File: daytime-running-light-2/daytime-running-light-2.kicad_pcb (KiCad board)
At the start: 2 copper layers, 57.8 x 87.8 mm, 58 parts, among them J1 Conn_01x01_Socket, J2 Conn_01x01_Socket, J3 Conn_01x01_Socket, J4 Conn_01x01_Socket, J5 Conn_01x01_Socket, J6 Conn_01x01_Pin, J7 Conn_01x01_Socket, J8 Conn_01x01_Socket, J9 Conn_01x01_Socket, Q1 BC548, Q2 IRF9540N, Q3 IRFB3004PbF, SW1 SW_SPST, U1 L7812, U2 TLC555xP, U3 L7812, U4 4001, U5 4069, U6 IRS10752LPbF

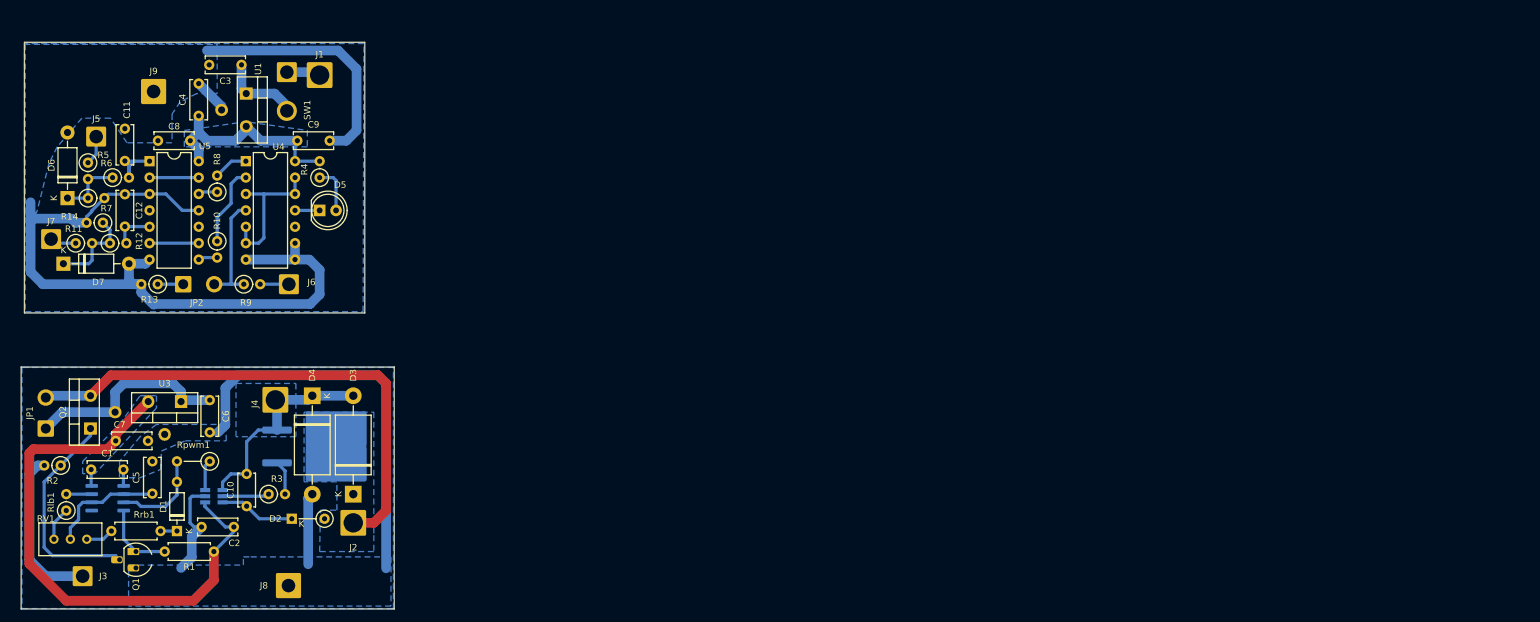
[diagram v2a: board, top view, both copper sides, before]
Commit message: [drl] Add proper voltage bootstrap powered from a double voltage. Start reimpl PCB
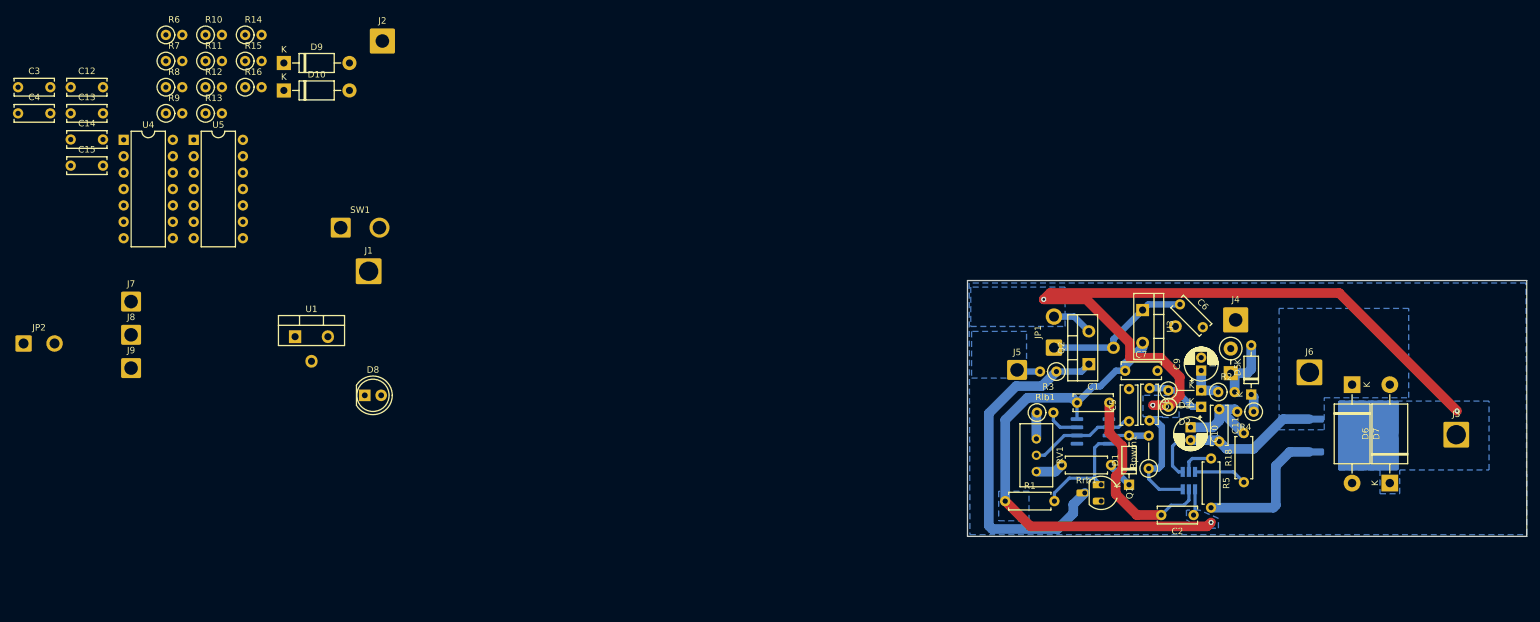
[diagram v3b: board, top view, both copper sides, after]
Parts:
- added C13: 0.1uF, Capacitor_THT:C_Disc_D6.0mm_W2.5mm_P5.00mm, F.Cu at (27.2, 29.7)
- added C14: 0.33uF, Capacitor_THT:C_Disc_D6.0mm_W2.5mm_P5.00mm, F.Cu at (27.2, 33.8)
- added C15: 0.33uF, Capacitor_THT:C_Disc_D6.0mm_W2.5mm_P5.00mm, F.Cu at (27.2, 37.8)
- added D10: 1N4742A, Diode_THT:D_DO-41_SOD81_P10.16mm_Horizontal, F.Cu at (60.2, 26.2)
- added D8: LED, LED_THT:LED_D5.0mm, F.Cu at (72.8, 73.4)
- added D9: 1N47xxA, Diode_THT:D_DO-41_SOD81_P10.16mm_Horizontal, F.Cu at (60.2, 21.9)
- added R15: R, Resistor_THT:R_Axial_DIN0207_L6.3mm_D2.5mm_P2.54mm_Vertical, F.Cu at (54.3, 21.6)
- added R16: 100k, Resistor_THT:R_Axial_DIN0207_L6.3mm_D2.5mm_P2.54mm_Vertical, F.Cu at (54.3, 25.7)
- added R18: 0R, Resistor_THT:R_Axial_DIN0207_L6.3mm_D2.5mm_P7.62mm_Horizontal, F.Cu at (208.9, 86.9)
- C10: value C -> 4.7uF; footprint Capacitor_THT:C_Disc_D5.0mm_W2.5mm_P5.00mm -> Capacitor_THT:CP_Radial_D5.0mm_P2.00mm
- C11: value 0.33uF -> 100nF
- C12: value 0.33uF -> 0.1uF
- C8: value 0.1uF -> 100nF
- C9: value 0.1uF -> 1uF; footprint Capacitor_THT:C_Disc_D6.0mm_W2.5mm_P5.00mm -> Capacitor_THT:CP_Radial_D5.0mm_P2.00mm
- D2: value 1N4148 -> BAT42
- D3: value 1.5KE18A -> BAT42; footprint Diode_THT:D_DO-201AE_P15.24mm_Horizontal -> Diode_THT:D_DO-35_SOD27_P5.08mm_Vertical_KathodeUp
- D4: value 1.5KE18A -> 1N4746A, 18V; footprint Diode_THT:D_DO-201AE_P15.24mm_Horizontal -> Diode_THT:D_DO-41_SOD81_P3.81mm_Vertical_KathodeUp
- D5: value LED -> 1N4148; footprint LED_THT:LED_D5.0mm -> Diode_THT:D_DO-35_SOD27_P7.62mm_Horizontal
- D6: value 1N47xxA -> 1.5KE18A; footprint Diode_THT:D_DO-41_SOD81_P10.16mm_Horizontal -> Diode_THT:D_DO-201AE_P15.24mm_Horizontal
- D7: value 1N4742A -> 1.5KE18A; footprint Diode_THT:D_DO-41_SOD81_P10.16mm_Horizontal -> Diode_THT:D_DO-201AE_P15.24mm_Horizontal
- J2, J4: footprint Connector_Wire:SolderWire-2.5sqmm_1x01_D2.4mm_OD3.6mm -> Connector_Wire:SolderWire-1.5sqmm_1x01_D1.7mm_OD3.9mm
- J3: footprint Connector_Wire:SolderWire-1.5sqmm_1x01_D1.7mm_OD3mm -> Connector_Wire:SolderWire-2.5sqmm_1x01_D2.4mm_OD3.6mm
- J6: value Conn_01x01_Pin -> Conn_01x01_Socket; footprint Connector_Wire:SolderWire-1.5sqmm_1x01_D1.7mm_OD3mm -> Connector_Wire:SolderWire-2.5sqmm_1x01_D2.4mm_OD3.6mm
- J8: value Conn_01x01_Socket -> Conn_01x01_Pin; footprint Connector_Wire:SolderWire-1.5sqmm_1x01_D1.7mm_OD3.9mm -> Connector_Wire:SolderWire-1.5sqmm_1x01_D1.7mm_OD3mm
- J9: footprint Connector_Wire:SolderWire-1.5sqmm_1x01_D1.7mm_OD3.9mm -> Connector_Wire:SolderWire-1.5sqmm_1x01_D1.7mm_OD3mm
- R11: value 1k -> 100
- R12: value 47k -> 1k
- R13: value R -> 1k
- R14: value 100k -> 47k
- R2: value 10k -> 1k
- R3: value 1k -> 10k
- R4: value R -> 51
- R5: footprint Resistor_THT:R_Axial_DIN0207_L6.3mm_D2.5mm_P2.54mm_Vertical -> Resistor_THT:R_Axial_DIN0207_L6.3mm_D2.5mm_P7.62mm_Horizontal
- R6: value 47k -> R
- R7: value 100k -> 1k
- R8: value 1k -> 47k
- R9: value 100 -> 100k
- moved J3 213.9 mm to (241.8, 79.5)
- moved D6 209.5 mm to (231.5, 87.0)
- moved D7 200.5 mm to (225.7, 71.8), turned to -90 degrees
- moved R5 179.9 mm to (203.8, 83.2)
- moved R2 179.6 mm to (204.9, 72.9), turned to 0 degrees
- moved C11 173.8 mm to (205.1, 75.6), turned to -90 degrees
- moved Q3 159.9 mm to (226.7, 79.6)
- moved J6 158.6 mm to (219.1, 69.8)
- moved C7 156.7 mm to (190.5, 69.6)
- moved JP1 156.6 mm to (179.5, 66.0)
- moved Q2 154.9 mm to (184.9, 68.6)
- moved C8 153.4 mm to (194.3, 72.3), turned to -90 degrees
- moved C1 153.0 mm to (183.1, 74.5)
- moved U2 152.9 mm to (185.5, 79.0)
- moved C5 151.7 mm to (191.1, 77.4)
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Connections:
- C10 pad 1: Net-(D2-K) -> /V_BOOTSTRAP
- C10 pad 2: /POWER_OUTPUT -> GND3
- C11 pad 1: Net-(C11-Pad1) -> /V_BOOTSTRAP
- C11 pad 2: GND -> GND3
- C12 pad 1: Net-(C12-Pad1) -> VCC
- C8 pad 1: VCC -> Net-(D2-K)
- C8 pad 2: GND -> /PWM
- C9 pad 1: VCC -> Net-(D3-K)
- C9 pad 2: GND -> GND2
- D3 pad 1: +BATT2 -> Net-(D3-K)
- D3 pad 2: /POWER_OUTPUT -> Net-(D2-K)
- D4 pad 1: /POWER_OUTPUT -> /DOUBLED_VCC2
- D5 pad 2: Net-(D5-A) -> /DOUBLED_VCC2
- D6 pad 1: Net-(D6-K) -> +BATT2
- D6 pad 2: GND -> GND3
- D7 pad 1: Net-(D7-K) -> GND3
- D7 pad 2: GND -> GND2
- J2 pad 1: +BATT2 -> GND
- J3 pad 1: Net-(J3-Pin_1) -> +BATT2
- J4 pad 1: /POWER_OUTPUT -> GND2
- J5 pad 1: /HEADLIGHT -> Net-(J5-Pin_1)
- J6 pad 1: Net-(J6-Pin_1) -> GND3
- J7 pad 1: /HIGHBEAM -> /HEADLIGHT
- J8 pad 1: GND2 -> Net-(J8-Pin_1)
- J9 pad 1: GND -> /HIGHBEAM
- Q3 pad 3: /POWER_OUTPUT -> GND3
- R11 pad 1: /HIGHBEAM -> Net-(JP2-B)
- R11 pad 2: Net-(D7-K) -> Net-(J8-Pin_1)
- R12 pad 1: Net-(D7-K) -> Net-(R12-Pad1)
- R12 pad 2: Net-(C12-Pad1) -> Net-(R12-Pad2)
- R13 pad 1: Net-(JP2-A) -> /HIGHBEAM
- R13 pad 2: GND -> Net-(D10-K)
- R14 pad 1: Net-(D7-K) -> Net-(D10-K)
- R14 pad 2: GND -> Net-(C15-Pad1)
- R2 pad 1: /ALLOW_POWER_ON -> Net-(D3-K)
- R2 pad 2: Net-(J3-Pin_1) -> /DOUBLED_VCC2
- R3 pad 1: Net-(U6-HO) -> /ALLOW_POWER_ON
- R3 pad 2: Net-(Q3-G) -> Net-(J5-Pin_1)
- R4 pad 1: Net-(D5-A) -> Net-(D5-K)
- R4 pad 2: VCC -> /V_BOOTSTRAP
- R5 pad 1: /HEADLIGHT -> Net-(U6-HO)
- R5 pad 2: Net-(D6-K) -> Net-(Q3-G)
- R6 pad 1: Net-(D6-K) -> Net-(D8-A)
- R6 pad 2: Net-(C11-Pad1) -> VCC
- R7 pad 1: Net-(D6-K) -> /HEADLIGHT
- R7 pad 2: GND -> Net-(D9-K)
- R8 pad 1: Net-(R8-Pad1) -> Net-(D9-K)
- R8 pad 2: Net-(R8-Pad2) -> Net-(C14-Pad1)
- R9 pad 1: Net-(JP2-B) -> Net-(D9-K)
- R9 pad 2: Net-(J6-Pin_1) -> GND
- U4 pad 1: Net-(R8-Pad2) -> Net-(R10-Pad2)
- U4 pad 11: Net-(D5-K) -> Net-(D8-K)
- U4 pad 2: Net-(R10-Pad1) -> Net-(R12-Pad1)
- U5 pad 1: Net-(C11-Pad1) -> Net-(C14-Pad1)
- U5 pad 12: Net-(R8-Pad1) -> Net-(R10-Pad1)
- U5 pad 5: Net-(C12-Pad1) -> Net-(C15-Pad1)
- U5 pad 8: Net-(R10-Pad2) -> Net-(R12-Pad2)
- U6 pad 4: /POWER_OUTPUT -> GND3
- U6 pad 6: Net-(D2-K) -> Net-(U6-VB)
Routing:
- net GND: track 161.6 -> 0.00 mm
- net GND2: track 93.3 -> 32.1 mm
- net /POWER_OUTPUT: track 35.7 -> 0.00 mm
- net VCC: track 33.7 -> 0.00 mm
- net +BATT2: track 81.4 -> 113.3 mm, vias 0 -> 3
- net GND3: track 0.00 -> 29.1 mm
- net Net-(J3-Pin_1): track 25.5 -> 0.00 mm
- net Net-(U4-Pad12): track 23.3 -> 0.00 mm
- net /ALLOW_POWER_ON: track 33.9 -> 54.3 mm
- net Net-(JP2-B): track 17.6 -> 0.00 mm
- net Net-(Q3-G): track 5.36 -> 22.4 mm
- net /V_BOOTSTRAP: track 0.00 -> 14.9 mm
- net Net-(D7-K): track 13.7 -> 0.00 mm
- net /PWM: track 4.75 -> 18.1 mm
- net Net-(SW1-B): track 12.6 -> 0.00 mm
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- added copper zone on B.Cu, net GND3
- added copper zone on B.Cu, net Net-(J5-Pin_1)
- removed copper zone on B.Cu, net (none)
- removed copper zone on B.Cu, net /POWER_OUTPUT
- removed copper zone on B.Cu, net GND
- removed copper zone on B.Cu, net VCC
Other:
- board size 57.8 x 87.8 mm -> 86.6 x 39.6 mm

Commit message: [drl] Finish PCB.
    TODO - fix DRC.
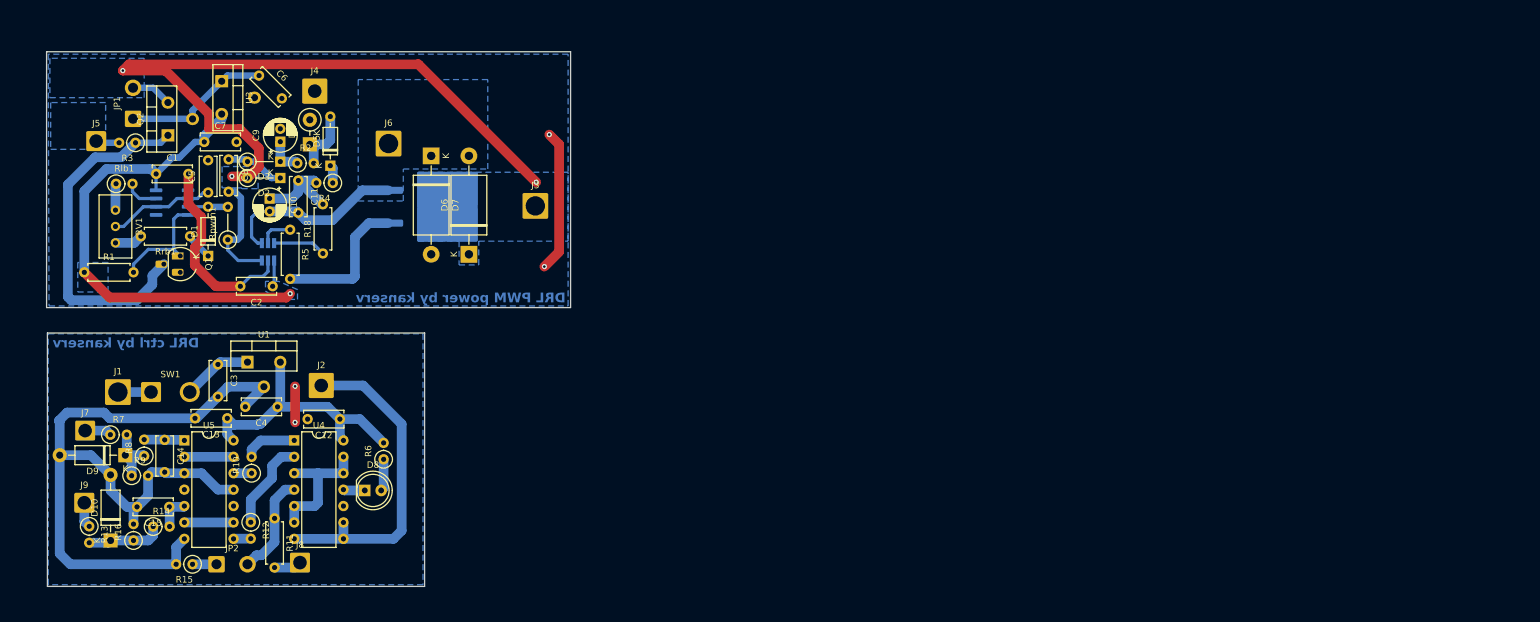
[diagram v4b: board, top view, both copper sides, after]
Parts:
- D9: value 1N47xxA -> 1N4742A
- R11: footprint Resistor_THT:R_Axial_DIN0207_L6.3mm_D2.5mm_P2.54mm_Vertical -> Resistor_THT:R_Axial_DIN0207_L6.3mm_D2.5mm_P7.62mm_Horizontal
- moved C6 147.0 mm to (56.4, 23.9)
- moved C8 147.0 mm to (51.7, 36.9)
- moved C9 147.0 mm to (59.7, 34.1)
- moved D2 147.0 mm to (59.7, 39.8)
- moved D3 147.0 mm to (59.7, 37.2)
- moved D4 147.0 mm to (64.3, 34.5)
- moved J4 147.0 mm to (65.0, 26.3)
- moved Q1 147.0 mm to (44.2, 51.8)
- moved Q2 147.0 mm to (42.3, 33.1)
- moved R1 147.0 mm to (29.3, 54.4)
- moved R2 147.0 mm to (62.3, 37.5)
- moved R5 147.0 mm to (61.2, 47.8)
- moved Rlb1 147.0 mm to (34.3, 40.6)
- moved Rrb1 147.0 mm to (45.7, 48.8)
- moved U3 147.0 mm to (50.6, 24.8)
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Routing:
- net GND: track 0.00 -> 179.2 mm, vias 0 -> 2
- net VCC: track 0.00 -> 42.6 mm
- net GND2: track 32.1 -> 54.1 mm, vias 0 -> 2
- net Net-(U4-Pad12): track 0.00 -> 21.2 mm
- net Net-(JP2-B): track 0.00 -> 15.8 mm
- net Net-(R12-Pad1): track 0.00 -> 14.1 mm
- net Net-(D10-K): track 0.00 -> 11.8 mm
- net Net-(SW1-B): track 0.00 -> 10.9 mm
- net Net-(D9-K): track 0.00 -> 9.83 mm
- net Net-(R10-Pad2): track 0.00 -> 8.33 mm
- net Net-(U5-Pad6): track 0.00 -> 7.62 mm
- net Net-(U5-Pad13): track 0.00 -> 7.62 mm
- net Net-(C14-Pad1): track 0.00 -> 6.28 mm
- net Net-(C15-Pad1): track 0.00 -> 5.44 mm
- net +BATT: track 0.00 -> 5.13 mm
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- added copper zone on B.Cu, net GND
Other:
- board size 86.6 x 39.6 mm -> 81.2 x 82.8 mm
- board text added: "DRL PWM power by kanserv"
- board text added: "DRL ctrl by kanserv"

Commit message: [drl] Fix design rules check
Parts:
- D3: footprint Diode_THT:D_DO-35_SOD27_P5.08mm_Vertical_KathodeUp -> Diode_THT:D_DO-35_SOD27_P5.08mm_Vertical_AnodeUp
- moved D3 0.28 mm to (59.4, 37.2)
- moved U5 0.13 mm to (44.8, 80.3)
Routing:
- net GND: track 179.2 -> 6.03 mm
- added copper zone on B.Cu, net +BATT
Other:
- board text added: "DRL PWM power"
- board text added: "DRL ctrl"
- board text removed: "DRL PWM power by kanserv"
- board text removed: "DRL ctrl by kanserv"

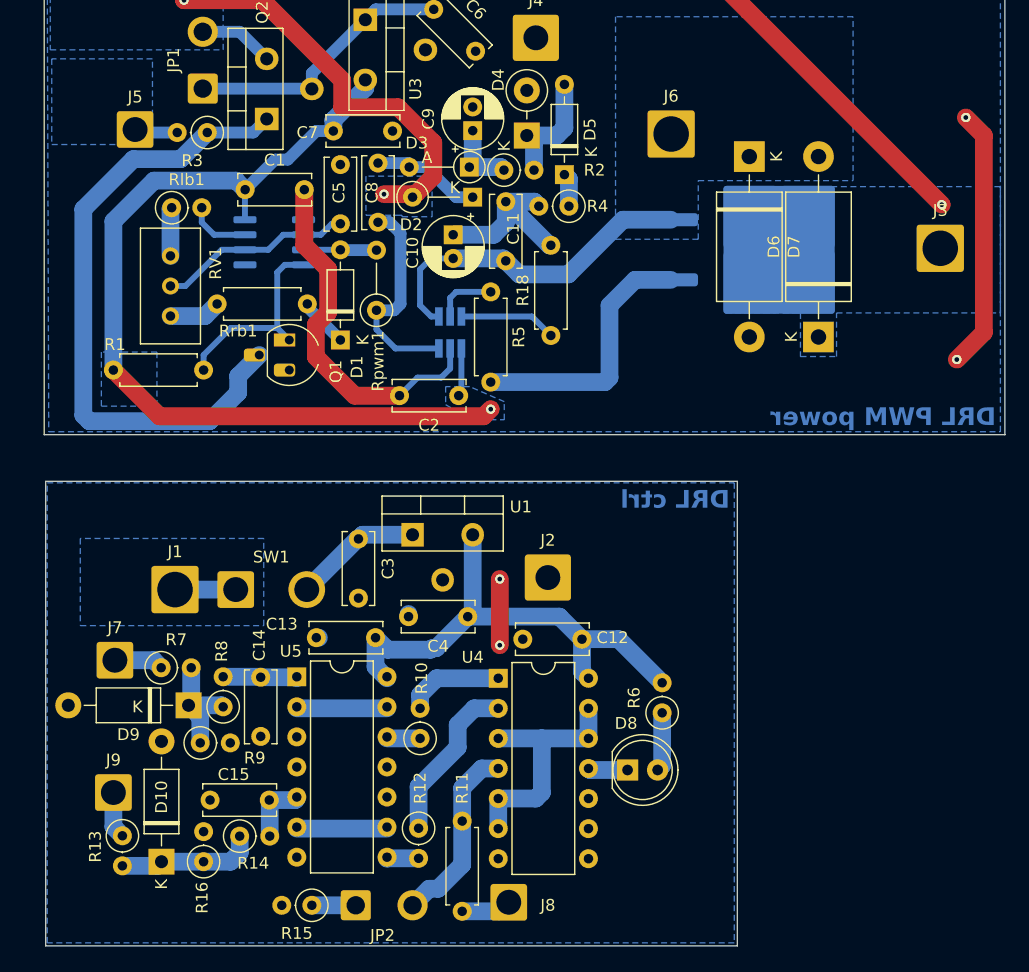
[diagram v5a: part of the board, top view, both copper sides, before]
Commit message: [drl] Update some zones and traces on PCB. Fix DRC. Reduce size of ctrl PCB. Add zones for headlight and highbeam connection.
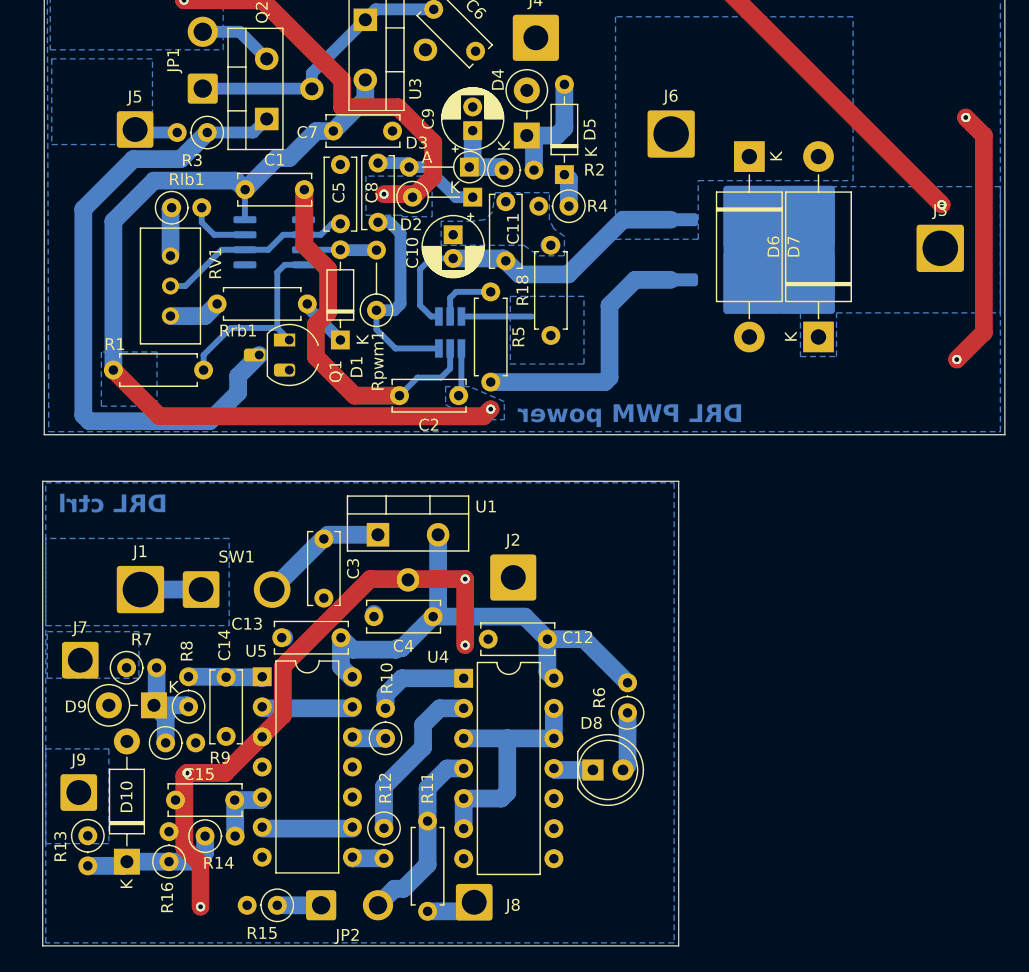
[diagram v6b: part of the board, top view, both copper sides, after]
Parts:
- D9: footprint Diode_THT:D_DO-41_SOD81_P10.16mm_Horizontal -> Diode_THT:D_DO-41_SOD81_P3.81mm_Vertical_KathodeUp
- moved C12 2.92 mm to (66.0, 77.1)
- moved D8 2.92 mm to (69.8, 88.1)
- moved J2 2.92 mm to (63.1, 71.9)
- moved U5 2.92 mm to (41.9, 80.3)
- moved D10 2.92 mm to (30.5, 95.9)
- moved C13 2.92 mm to (48.6, 77.0)
- moved C14 2.92 mm to (38.9, 80.3)
- moved C15 2.92 mm to (39.6, 90.7)
- moved C3 2.92 mm to (47.1, 68.6)
- moved C4 2.92 mm to (56.3, 75.2)
- moved D9 2.92 mm to (32.8, 82.7)
- moved J7 2.92 mm to (26.5, 78.9)
- moved J8 2.92 mm to (59.8, 99.3)
- moved J9 2.92 mm to (26.4, 90.0)
- moved JP2 2.92 mm to (46.9, 99.6)
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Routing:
- net GND: track 6.03 -> 50.7 mm, vias 2 -> 4
- net /V_BOOTSTRAP: track 14.9 -> 0.13 mm
- net /HEADLIGHT: track 4.17 -> 0.00 mm
- net /HIGHBEAM: track 3.97 -> 0.00 mm
- net Net-(U6-VB): track 8.22 -> 5.95 mm
- added copper zone on B.Cu, net /HEADLIGHT
- added copper zone on B.Cu, net /HIGHBEAM
- added copper zone on B.Cu, net /V_BOOTSTRAP
- added copper zone on B.Cu, net Net-(U6-VB)
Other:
- board size 81.2 x 82.8 mm -> 81.3 x 82.8 mm
